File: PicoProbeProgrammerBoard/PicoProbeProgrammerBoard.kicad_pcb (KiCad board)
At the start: 2 copper layers, 43.2 x 27.9 mm, 7 parts, among them J1 Conn_02x05_Odd_Even, J2 Conn_01x07_Male, J3 Conn_02x03_Odd_Even, J4 BM03B-SRSS-TBLFSN, U1 Pico

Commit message: added schematic for raspberry pi
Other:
- board size 43.2 x 27.9 mm -> 27.9 x 73.3 mm
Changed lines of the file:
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@@
     )
   )
-  (gr_line (start 109.22 76.2) (end 152.4 68.58) (layer "Edge.Cuts") (width 0.1))
-  (gr_line (start 109.22 96.52) (end 109.22 76.2) (layer "Edge.Cuts") (width 0.1))
-  (gr_line (start 152.4 68.58) (end 152.4 96.52) (layer "Edge.Cuts") (width 0.1))
-  (gr_line (start 152.4 96.52) (end 109.22 96.52) (layer "Edge.Cuts") (width 0.1))
+  (gr_rect (start 114.625 19.2) (end 142.575 92.55) (layer "Edge.Cuts") (width 0.1) (fill none))
 )

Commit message: almost done the board layout
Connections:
- J1 pad 3: Earth -> GND
- J2 pad 3: Earth -> GND
- J3 pad 2: /SW0 -> /SWO
- J4 pad 2: Earth -> GND
- U1 pad 13: unconnected-(U1-Pad13) -> GND
- U1 pad 18: unconnected-(U1-Pad18) -> GND
- U1 pad 23: unconnected-(U1-Pad23) -> GND
- U1 pad 28: unconnected-(U1-Pad28) -> GND
- U1 pad 8: Earth -> GND
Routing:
- net /SDA_0: track 0.00 -> 93.2 mm, vias 0 -> 3
- net /SWDIO: track 0.00 -> 87.1 mm, vias 0 -> 2
- net /SWDCLK: track 0.00 -> 82.4 mm, vias 0 -> 2
- net /SCL_0: track 0.00 -> 82.0 mm, vias 0 -> 2
- net /SWO: track 0.00 -> 78.7 mm, vias 0 -> 3
- net Net-(JP1-Pad1): track 0.00 -> 60.1 mm, vias 0 -> 2
- net Net-(JP2-Pad1): track 0.00 -> 55.7 mm, vias 0 -> 2
- net /SDA_1: track 0.00 -> 23.1 mm
- net /power_output: track 0.00 -> 20.7 mm, vias 0 -> 2
- net /UartTX: track 0.00 -> 19.1 mm
- net /SCL_1: track 0.00 -> 18.4 mm
- net GND: track 0.00 -> 1.55 mm, vias 0 -> 1
- added copper zone on B.Cu, net GND
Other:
- board size 27.9 x 73.3 mm -> 27.9 x 74.8 mm

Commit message: board sent out
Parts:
- J1: value Conn_02x05_Odd_Even -> PicoDebugPlus_V0.1
- J4: value BM03B-SRSS-TBLFSN -> JST_SWD
- renumbered JP2 to 3v3, JP1 to 5v, J3 to ExtraConns
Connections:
- J4 pad 4: (no net) -> GND
- J4 pad 5: (no net) -> GND
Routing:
- net GND: track 1.55 -> 3.65 mm, vias 1 -> 2
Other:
- board text added: "IC1 D/C IC0 D/C Uart T/R"
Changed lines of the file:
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@@
       (psa4output false)
       (plotreference true)
-      (plotvalue true)
+      (plotvalue false)
       (plotinvisibletext false)
       (sketchpadsonfab false)
@@
       (outputformat 1)
       (mirror false)
-      (drillshape 1)
+      (drillshape 0)
       (scaleselection 1)
-      (outputdirectory "")
+      (outputdirectory "gerber/")
     )
   )
@@
       (effects (font (size 1 1) (thickness 0.15)))
     )
-    (fp_text value "BM03B-SRSS-TBLFSN" (at 0 -1.4284) (layer "F.SilkS")
+    (fp_text value "JST_SWD" (at 0 -4.094) (layer "F.SilkS")
       (effects (font (size 1 1) (thickness 0.15)))
     )
@@
     (pad "3" smd rect locked (at -1.000001 -1.4284) (size 0.6604 1.5494) (layers "F.Cu" "F.Paste" "F.Mask")
       (net 6 "/SWDCLK") (pinfunction "3") (pintype "unspecified"))
-    (pad "4" smd rect locked (at -2.3 1.096599 90) (size 1.905 1.2954) (layers "F.Cu" "F.Paste" "F.Mask"))
-    (pad "5" smd rect locked (at 2.3 1.096599 90) (size 1.905 1.2954) (layers "F.Cu" "F.Paste" "F.Mask"))
+    (pad "4" smd rect locked (at -2.3 1.096599 90) (size 1.905 1.2954) (layers "F.Cu" "F.Paste" "F.Mask")
+      (net 5 "GND"))
+    (pad "5" smd rect locked (at 2.3 1.096599 90) (size 1.905 1.2954) (layers "F.Cu" "F.Paste" "F.Mask")
+      (net 5 "GND"))
   )
   (footprint "Connector_PinSocket_2.54mm:PinSocket_2x03_P2.54mm_Vertical" (layer "F.Cu")
@@
     (property "Sheetname" "")
     (attr through_hole)
-    (fp_text reference "J3" (at -1.27 -2.77 180) (layer "F.SilkS")
-      (effects (font (size 1 1) (thickness 0.15)))
-    )
-    (fp_text value "Conn_02x03_Odd_Even" (at -1.27 7.85 180) (layer "F.Fab")
+    (fp_text reference "ExtraConns" (at -1.27 -2.77 180) (layer "F.SilkS")
+      (effects (font (size 1 1) (thickness 0.15)))
+    )
+    (fp_text value "Conn_02x03_Odd_Even" (at -6.3246 7.8232 180) (layer "F.Fab")
       (effects (font (size 1 1) (thickness 0.15)))
     )
@@
     (property "Sheetname" "")
     (attr through_hole)
-    (fp_text reference "JP2" (at 0 -2.33) (layer "F.SilkS")
+    (fp_text reference "3v3" (at 0 -2.33) (layer "F.SilkS")
       (effects (font (size 1 1) (thickness 0.15)))
     )
@@
     (property "Sheetname" "")
     (attr through_hole)
-    (fp_text reference "JP1" (at 0 -2.33) (layer "F.SilkS")
-      (effects (font (size 1 1) (thickness 0.15)))
-    )
-    (fp_text value "Jumper_2_Open" (at 0 4.87) (layer "F.Fab")
+    (fp_text reference "5v" (at 0.1524 -2.0828) (layer "F.SilkS")
+      (effects (font (size 1 1) (thickness 0.15)))
+    )
+    (fp_text value "Jumper_2_Open" (at 3.6576 4.6736) (layer "F.Fab")
       (effects (font (size 1 1) (thickness 0.15)))
     )
@@
       (effects (font (size 1 1) (thickness 0.15)))
     )
-    (fp_text value "Conn_02x05_Odd_Even" (at 0.381 4.318) (layer "F.SilkS")
+    (fp_text value "PicoDebugPlus_V0.1" (at 1.397 4.1532) (layer "F.SilkS")
       (effects (font (size 1 1) (thickness 0.15)))
     )
@@
   )
   (gr_rect (start 114.625 19.2) (end 142.575 94.0232) (layer "Edge.Cuts") (width 0.1) (fill none))
+  (gr_text "IC1 D/C\nIC0 D/C\nUart T/R\n" (at 139.3444 77.978) (layer "F.Adhes")
+    (effects (font (size 0.8 0.8) (thickness 0.15)))
+  )
+  (dimension (type aligned) (layer "Eco1.User")
+    (pts (xy 114.7064 95.9104) (xy 142.6972 96.266))
+    (height 0.005162)
+    (gr_text "27.9931 mm" (at 128.716343 94.943455 359.2721436) (layer "Eco1.User")
+      (effects (font (size 1 1) (thickness 0.15)))
+    )
+    (format (units 3) (units_format 1) (precision 4))
+    (style (thickness 0.15) (arrow_length 1.27) (text_position_mode 0) (extension_height 0.58642) (extension_offset 0.5) keep_text_aligned)
+  )
+  (dimension (type aligned) (layer "Eco1.User")
+    (pts (xy 144.1196 19.1516) (xy 144.2212 94.0308))
+    (height -0.914399)
+    (gr_text "74.8793 mm" (at 146.234797 56.588399 270.0777419) (layer "Eco1.User")
+      (effects (font (size 1 1) (thickness 0.15)))
+    )
+    (format (units 3) (units_format 1) (precision 4))
+    (style (thickness 0.15) (arrow_length 1.27) (text_position_mode 0) (extension_height 0.58642) (extension_offset 0.5) keep_text_aligned)
+  )
   (segment (start 128.5748 92.964) (end 132.2324 92.964) (width 0.25) (layer "F.Cu") (net 1))
   (segment (start 127.381 90.779) (end 127.381 91.7702) (width 0.25) (layer "F.Cu") (net 1))
@@
   (segment (start 121.4628 82.804) (end 118.618 82.804) (width 0.25) (layer "B.Cu") (net 4))
   (segment (start 127.508 88.8492) (end 136.0932 88.8492) (width 0.25) (layer "B.Cu") (net 4))
-  (segment (start 139.1 87.2332) (end 139.0904 87.2236) (width 0.25) (layer "F.Cu") (net 5))
-  (segment (start 139.1 88.7716) (end 139.1 87.2332) (width 0.25) (layer "F.Cu") (net 5))
-  (via (at 139.0904 87.2236) (size 0.8) (drill 0.4) (layers "F.Cu" "B.Cu") (net 5))
+  (segment (start 126.111 92.9386) (end 126.1364 92.964) (width 0.25) (layer "F.Cu") (net 5))
+  (segment (start 139.1 88.7716) (end 139.1 87.3348) (width 0.25) (layer "F.Cu") (net 5))
+  (segment (start 126.111 90.779) (end 126.111 92.9386) (width 0.25) (layer "F.Cu") (net 5))
+  (segment (start 139.1 87.3348) (end 139.0904 87.3252) (width 0.25) (layer "F.Cu") (net 5))
+  (via (at 126.1364 92.964) (size 0.8) (drill 0.4) (layers "F.Cu" "B.Cu") (net 5))
+  (via (at 139.0904 87.3252) (size 0.8) (drill 0.4) (layers "F.Cu" "B.Cu") (net 5))
   (segment (start 115.7732 31.1168) (end 118.25 28.64) (width 0.25) (layer "F.Cu") (net 6))
   (segment (start 115.7732 76.2) (end 115.7732 31.1168) (width 0.25) (layer "F.Cu") (net 6))
@@
   (zone (net 5) (net_name "GND") (layer "B.Cu") (hatch edge 0.508)
     (connect_pads (clearance 0.508))
-    (min_thickness 0.254)
-    (fill (thermal_gap 0.508) (thermal_bridge_width 0.508))
+    (min_thickness 0.254) (filled_areas_thickness no)
+    (fill yes (thermal_gap 0.508) (thermal_bridge_width 0.508))
     (polygon
       (pts
-        (xy 142.5448 94.0308)
-        (xy 114.6048 94.0308)
-        (xy 114.6048 19.2024)
-        (xy 142.5956 19.2024)
+        (xy 142.495242 94.08136)
+        (xy 114.555242 94.08136)
+        (xy 114.555242 19.25296)
+        (xy 142.546042 19.25296)
       )
     )

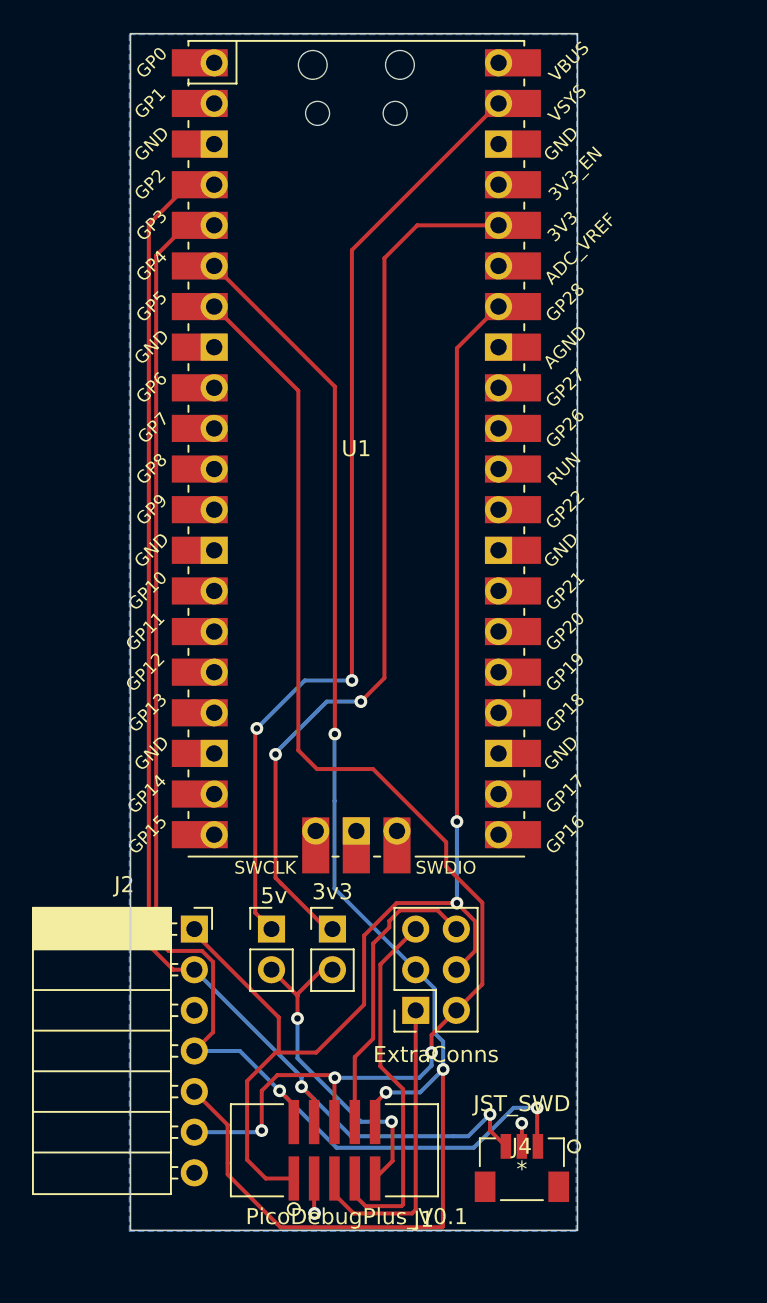
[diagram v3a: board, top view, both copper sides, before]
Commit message: pushed fix for the connector so it a staight through cable
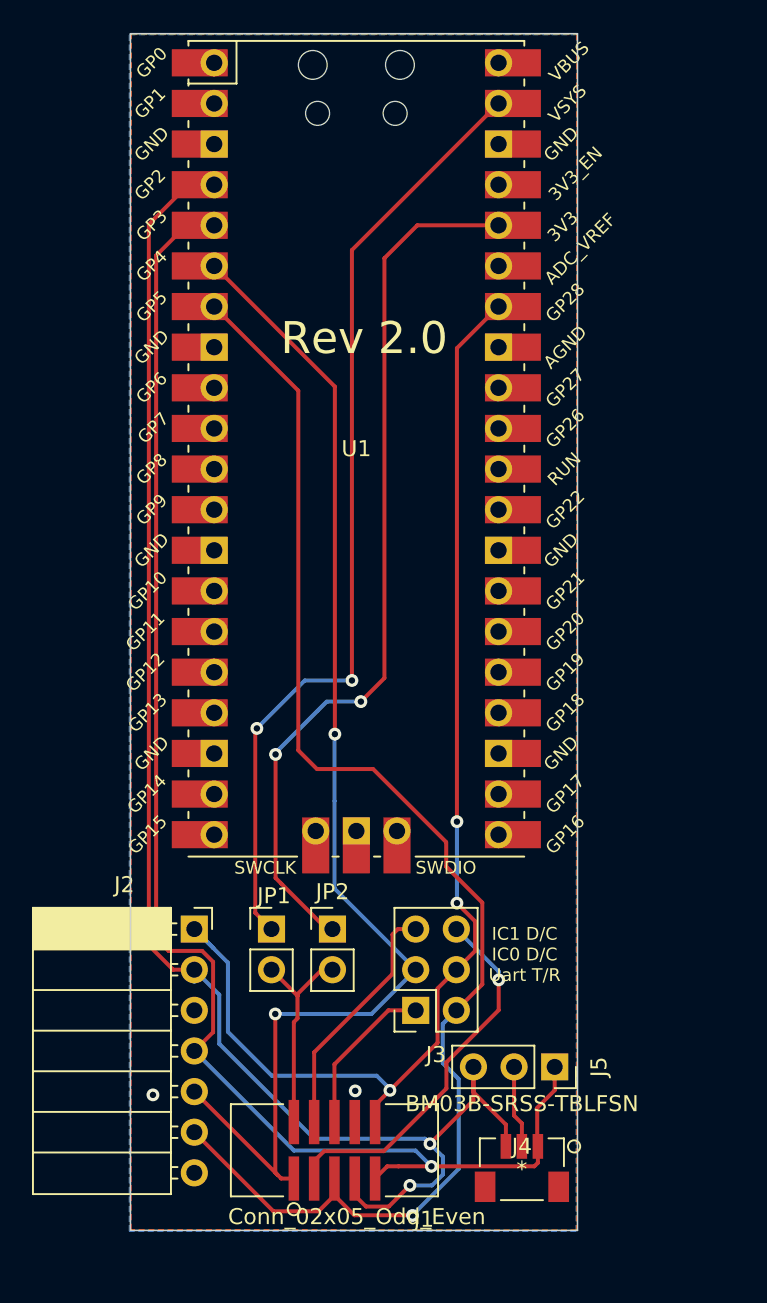
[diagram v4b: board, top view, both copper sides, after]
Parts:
- added J5: Conn_01x03_Male, Connector_PinSocket_2.54mm:PinSocket_1x03_P2.54mm_Vertical, F.Cu at (141.2, 83.8)
- J1: value PicoDebugPlus_V0.1 -> Conn_02x05_Odd_Even
- J4: value JST_SWD -> BM03B-SRSS-TBLFSN
- renumbered ExtraConns to J3, 5v to JP1, 3v3 to JP2
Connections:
- J1 pad 1: /SCL_0 -> /SDA_0
- J1 pad 10: /SDA_0 -> /SCL_0
- J1 pad 2: /SWDIO -> /power_output
- J1 pad 3: GND -> /SCL_1
- J1 pad 4: /SWDCLK -> /SDA_1
- J1 pad 5: /UartTX -> /SWO
- J1 pad 6: /SWO -> /UartTX
- J1 pad 7: /SDA_1 -> /SWDCLK
- J1 pad 8: /SCL_1 -> GND
- J1 pad 9: /power_output -> /SWDIO
- J4 pad 4: GND -> (no net)
- J4 pad 5: GND -> (no net)
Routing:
- net /SDA_0: track 93.2 -> 77.7 mm, vias 3 -> 2
- net /SWDCLK: track 82.4 -> 97.4 mm
- net /UartTX: track 19.1 -> 10.1 mm
- net /SDA_1: track 23.1 -> 15.3 mm
- net /SWO: track 78.7 -> 86.2 mm, vias 3 -> 1
- net /power_output: track 20.7 -> 13.2 mm, vias 2 -> 0
- net /SCL_1: track 18.4 -> 24.8 mm, vias 0 -> 1
- net /SWDIO: track 87.1 -> 92.2 mm, vias 2 -> 1
- net /SCL_0: track 82.0 -> 77.2 mm, vias 2 -> 3
- net GND: track 3.65 -> 6.48 mm
- added copper zone on F.Cu, net GND
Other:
- board text added: "Rev 2.0"
